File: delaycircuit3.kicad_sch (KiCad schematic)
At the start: 20 parts, among them J1 Screw_Terminal_01x02, J2 Screw_Terminal_01x02, J3 Screw_Terminal_01x02, J5 Screw_Terminal_01x03, J6 Screw_Terminal_01x02, U1 CD4002BE, U2 NE555N, U3 CD4002BE, U4 CD4002BE, U5 CD4002BE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

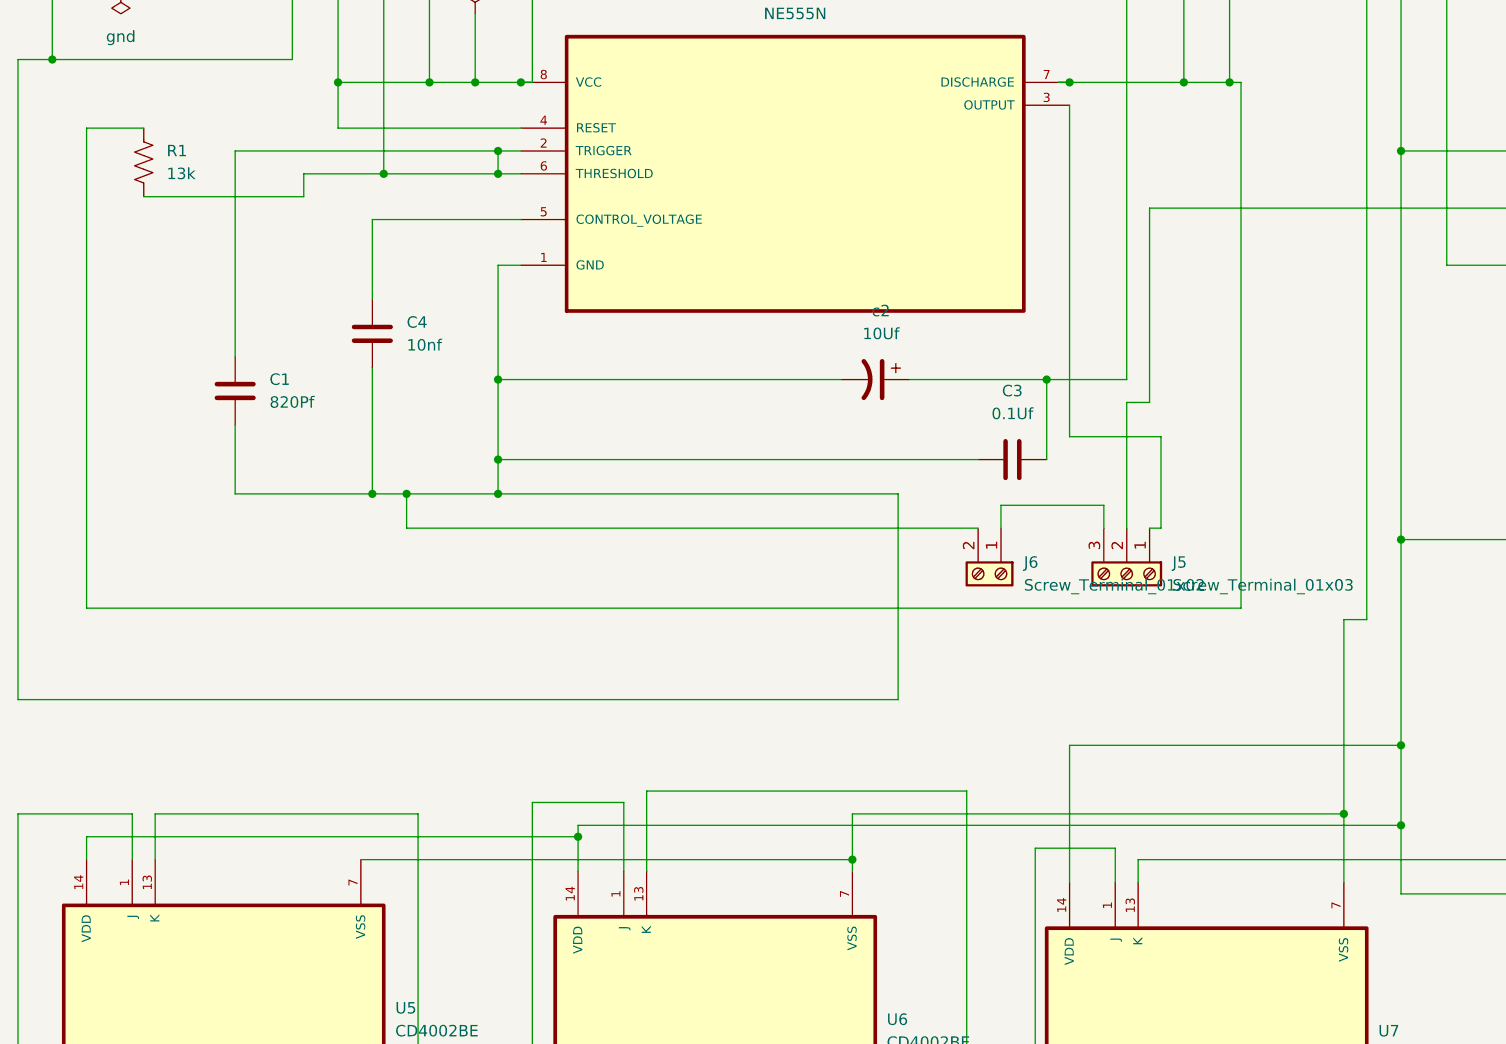
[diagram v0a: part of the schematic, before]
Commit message: resistencia en seire
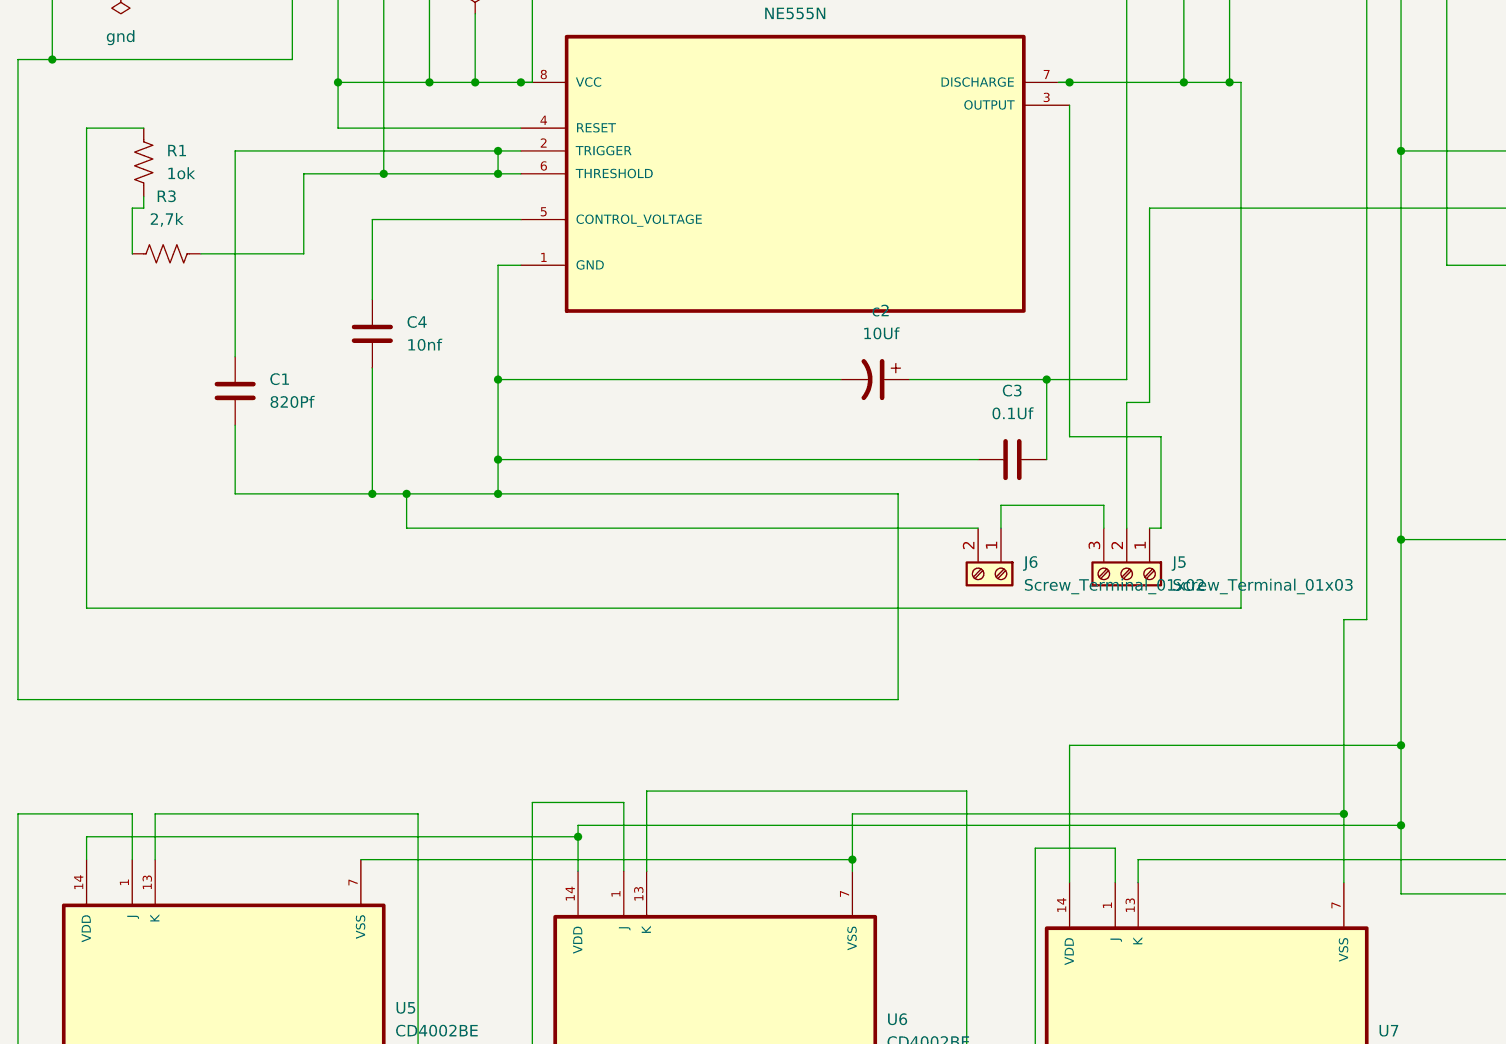
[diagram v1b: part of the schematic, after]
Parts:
- added R3: 2,7k, Resistor_THT:R_Axial_DIN0204_L3.6mm_D1.6mm_P7.62mm_Horizontal, symbol Device:R_US
- J6: footprint (none) -> TerminalBlock_Phoenix:TerminalBlock_Phoenix_MKDS-1,5-2-5.08_1x02_P5.08mm_Horizontal
- R1: value 13k -> 1ok
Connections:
- net at C1.1, D1.2 (A), U2.2 (TRIGGER)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: now also R3.2; no longer R1.1
- new net: R1.1, R3.1
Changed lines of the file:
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@@
 	(wire
 		(pts
-			(xy 45.72 59.69) (xy 45.72 57.15)
+			(xy 34.29 66.04) (xy 45.72 66.04)
+		)
+		(stroke
+			(width 0)
+			(type default)
+		)
+	)
+	(wire
+		(pts
+			(xy 26.67 60.96) (xy 27.94 60.96)
 		)
 		(stroke
@@
 	(wire
 		(pts
+			(xy 130.81 120.65) (xy 130.81 135.89)
+		)
+		(stroke
+			(width 0)
+			(type default)
+		)
+	)
+	(wire
+		(pts
 			(xy 139.7 60.96) (xy 260.35 60.96)
 		)
@@
 	(wire
 		(pts
-			(xy 130.81 135.89) (xy 130.81 120.65)
-		)
-		(stroke
-			(width 0)
-			(type default)
-		)
-	)
-	(wire
-		(pts
 			(xy 180.34 24.13) (xy 180.34 22.86)
 		)
@@
 	(wire
 		(pts
+			(xy 27.94 59.69) (xy 27.94 60.96)
+		)
+		(stroke
+			(width 0)
+			(type default)
+		)
+	)
+	(wire
+		(pts
 			(xy 123.19 93.98) (xy 134.62 93.98)
 		)
@@
 	(wire
 		(pts
-			(xy 367.03 100.33) (xy 377.19 100.33)
+			(xy 161.29 128.27) (xy 161.29 135.89)
 		)
 		(stroke
@@
 	(wire
 		(pts
-			(xy 189.23 16.51) (xy 339.09 16.51)
+			(xy 367.03 100.33) (xy 377.19 100.33)
 		)
 		(stroke
@@
 	(wire
 		(pts
-			(xy 163.83 17.78) (xy 163.83 19.05)
+			(xy 189.23 16.51) (xy 339.09 16.51)
 		)
 		(stroke
@@
 	(wire
 		(pts
-			(xy 27.94 59.69) (xy 45.72 59.69)
+			(xy 163.83 17.78) (xy 163.83 19.05)
 		)
 		(stroke
@@
 	(wire
 		(pts
-			(xy 232.41 92.71) (xy 238.76 92.71)
+			(xy 26.67 66.04) (xy 26.67 60.96)
 		)
 		(stroke
@@
 	(wire
 		(pts
-			(xy 184.15 54.61) (xy 184.15 48.26)
+			(xy 232.41 92.71) (xy 238.76 92.71)
 		)
 		(stroke
@@
 	(wire
 		(pts
-			(xy 238.76 77.47) (xy 238.76 74.93)
+			(xy 184.15 54.61) (xy 184.15 48.26)
 		)
 		(stroke
@@
 	(wire
 		(pts
-			(xy 233.68 124.46) (xy 242.57 124.46)
+			(xy 238.76 77.47) (xy 238.76 74.93)
 		)
 		(stroke
@@
 	(wire
 		(pts
-			(xy 161.29 135.89) (xy 161.29 128.27)
+			(xy 233.68 124.46) (xy 242.57 124.46)
 		)
 		(stroke
@@
 	(wire
 		(pts
+			(xy 45.72 57.15) (xy 45.72 66.04)
+		)
+		(stroke
+			(width 0)
+			(type default)
+		)
+	)
+	(wire
+		(pts
 			(xy 163.83 19.05) (xy 163.83 106.68)
 		)
@@
 			)
 		)
-		(property "Value" "13k"
+		(property "Value" "1ok"
 			(at 30.48 57.15 0)
 			(effects
@@
 			)
 		)
-		(property "Footprint" ""
+		(property "Footprint" "TerminalBlock_Phoenix:TerminalBlock_Phoenix_MKDS-1,5-2-5.08_1x02_P5.08mm_Horizontal"
 			(at 123.19 101.6 0)
 			(effects
@@
 					(unit 1)
 				)
+			)
+		)
+	)
+	(symbol
+		(lib_id "Device:R_US")
+		(at 30.48 66.04 90)
+		(unit 1)
+		(exclude_from_sim no)
+		(in_bom yes)
+		(on_board yes)
+		(dnp no)
+		(fields_autoplaced yes)
+		(property "Reference" "R3"
+			(at 30.48 59.69 90)
+			(effects
+				(font
+					(size 1.27 1.27)
+				)
+			)
+		)
+		(property "Value" "2,7k"
+			(at 30.48 62.23 90)
+			(effects
+				(font
+					(size 1.27 1.27)
+				)
+			)
+		)
+		(property "Footprint" "Resistor_THT:R_Axial_DIN0204_L3.6mm_D1.6mm_P7.62mm_Horizontal"
+			(at 30.734 65.024 90)
+			(effects
+				(font
+					(size 1.27 1.27)
+				)
+				(hide yes)
+			)
+		)
+		(property "Datasheet" "~"
+			(at 30.48 66.04 0)
+			(effects
+				(font
+					(size 1.27 1.27)
+				)
+				(hide yes)
+			)
+		)
+		(property "Description" "Resistor, US symbol"
+			(at 30.48 66.04 0)
+			(effects
+				(font
+					(size 1.27 1.27)
+				)
+				(hide yes)
+			)
+		)
+		(pin "1"
+		)
+		(pin "2"
+		)
+		(instances
+			(project ""
+				(path "/13b24ef1-8c89-41a3-8b79-9cbc78fc8d67"
+					(reference "R3")
+					(unit 1)
+				)
